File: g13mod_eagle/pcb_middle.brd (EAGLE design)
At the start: 134.2 x 33.2 mm, 80 parts

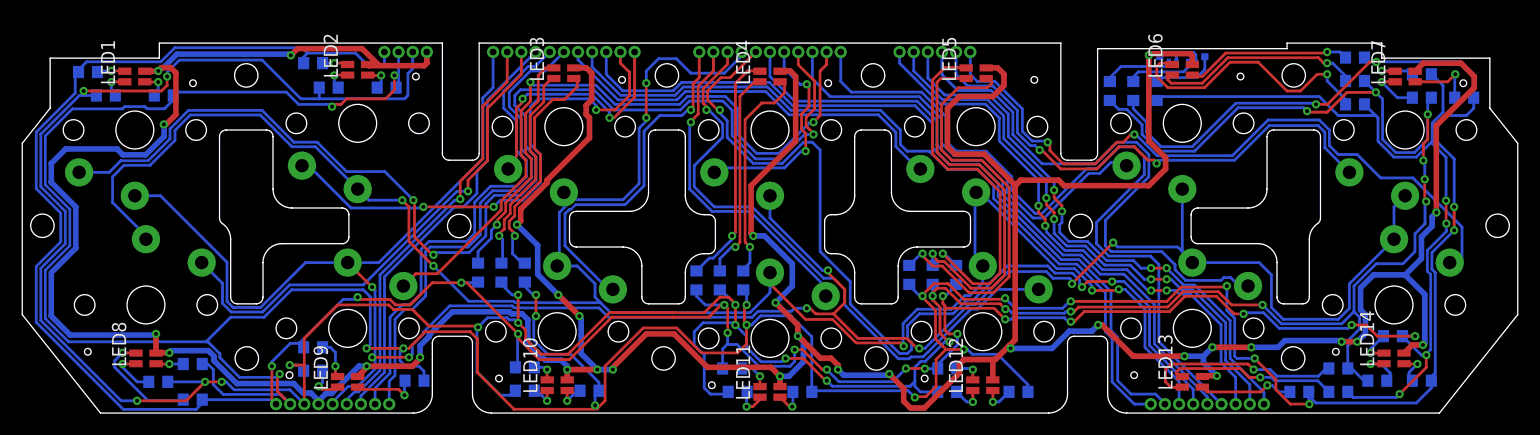
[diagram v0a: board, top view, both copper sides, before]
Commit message: Fix LED color
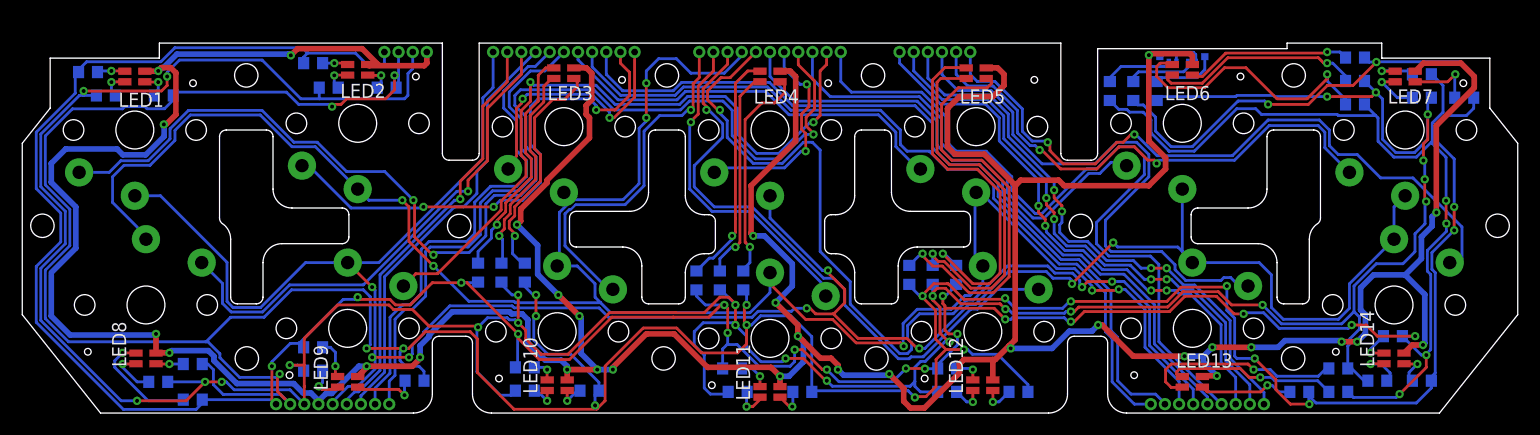
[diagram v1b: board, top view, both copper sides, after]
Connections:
- net B: now also R43.1; no longer R44.1
- net G: now also R44.1; no longer R43.1
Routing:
- net G: track 326.0 -> 317.3 mm
- net B: track 300.3 -> 308.0 mm
